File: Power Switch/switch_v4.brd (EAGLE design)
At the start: 25.7 x 14 mm, 27 parts, among them U2 ATTINY10-TS8R

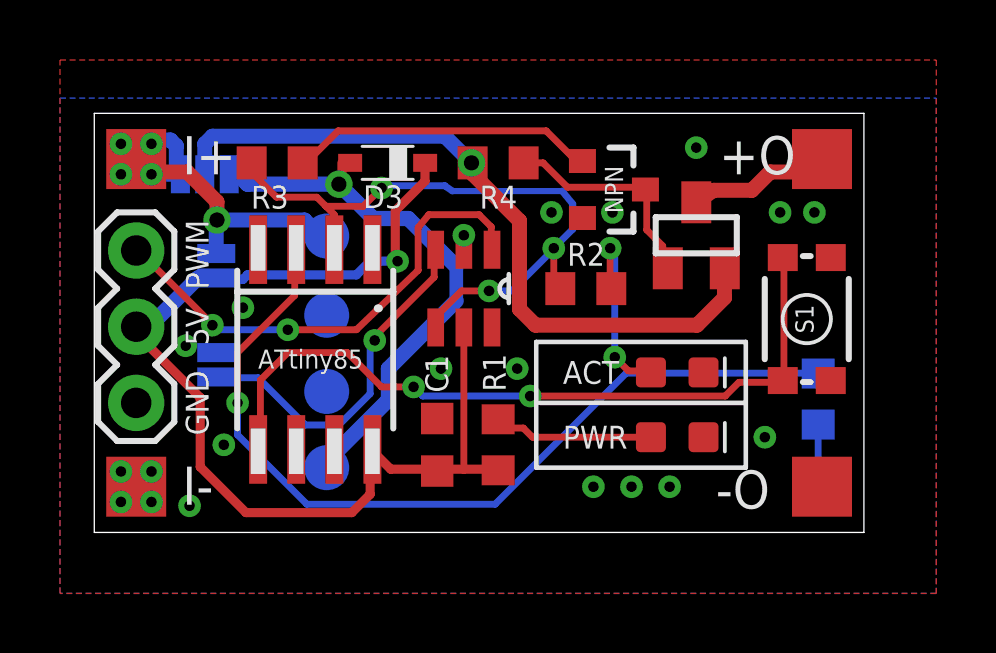
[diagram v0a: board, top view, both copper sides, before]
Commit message: PCB updates (jumper distance) and a new RGB mini board
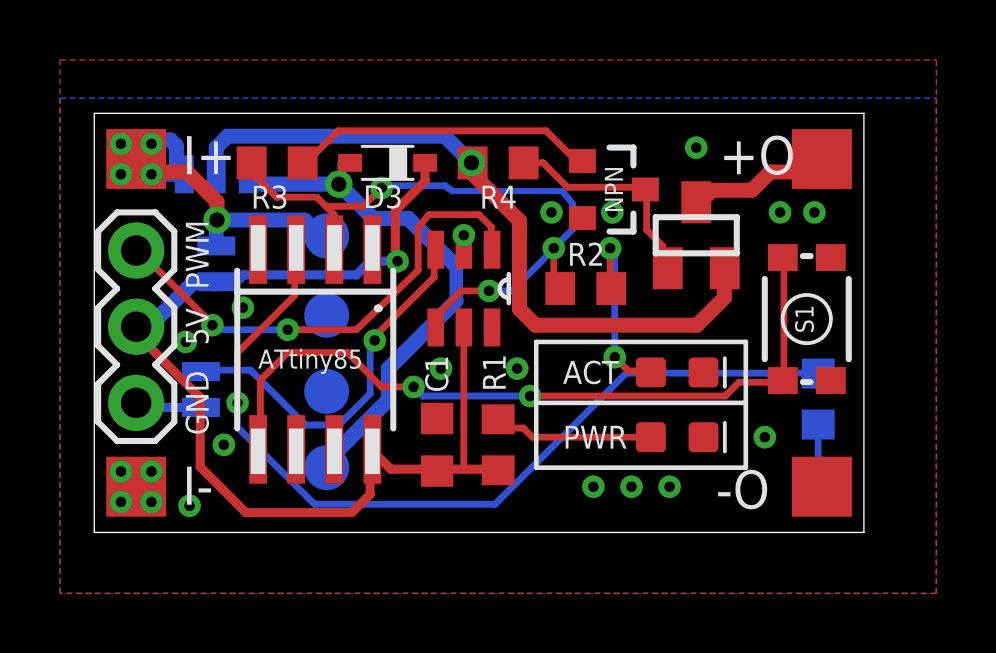
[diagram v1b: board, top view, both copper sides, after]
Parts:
- removed INV, INV1: PWM INV JUMPER, SparkFun-Jumpers:SMT-JUMPER_2_NO_NO-SILK
- added JP2: JUMPER-SMT_3_NO_NO-SILK, SparkFun-Jumpers:SMT-JUMPER_3_NO_NO-SILK
- added JP3: JUMPER-SMT_2_NO_NO-SILK, SparkFun-Jumpers:SMT-JUMPER_2_NO_NO-SILK
- JP1: value JUMPER-SMT_3_2-NC_PASTE_NO-SILK -> JUMPER-SMT_2_NO_NO-SILK; device SparkFun-Jumpers:SMT-JUMPER_3_2-NC_PASTE_NO-SILK -> SparkFun-Jumpers:SMT-JUMPER_2_NO_NO-SILK
- moved JP1 3.07 mm to (3.94, 96.0), turned to 270 degrees
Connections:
- net 5V: now also JP1.2; no longer INV1.2
- net GND: now also JP3.1; no longer INV.1
- net IN: now also JP2.2; no longer JP1.2
- net INV: now also JP3.2; no longer INV.2
- net REG_OUT: now also JP2.3; no longer JP1.3
- net VCC: now also JP2.1; no longer INV1.1
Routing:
- net GND: track 0.00 -> 2.22 mm
- net INV: track 12.0 -> 12.7 mm
- net REG_OUT: track 18.4 -> 17.8 mm
